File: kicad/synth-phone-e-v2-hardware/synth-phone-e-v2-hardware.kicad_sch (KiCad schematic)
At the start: 29 parts, among them J1 AudioJack4, J10 Audio_out_input, J11 mic_gain_input, J13 Audio_in_output, J14 Audio_out_output, J15 encoder_input, J2 AudioJack4, J3 DIN-5, J4 Keypad_column_output, J6 USB_C_Receptacle_USB2.0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

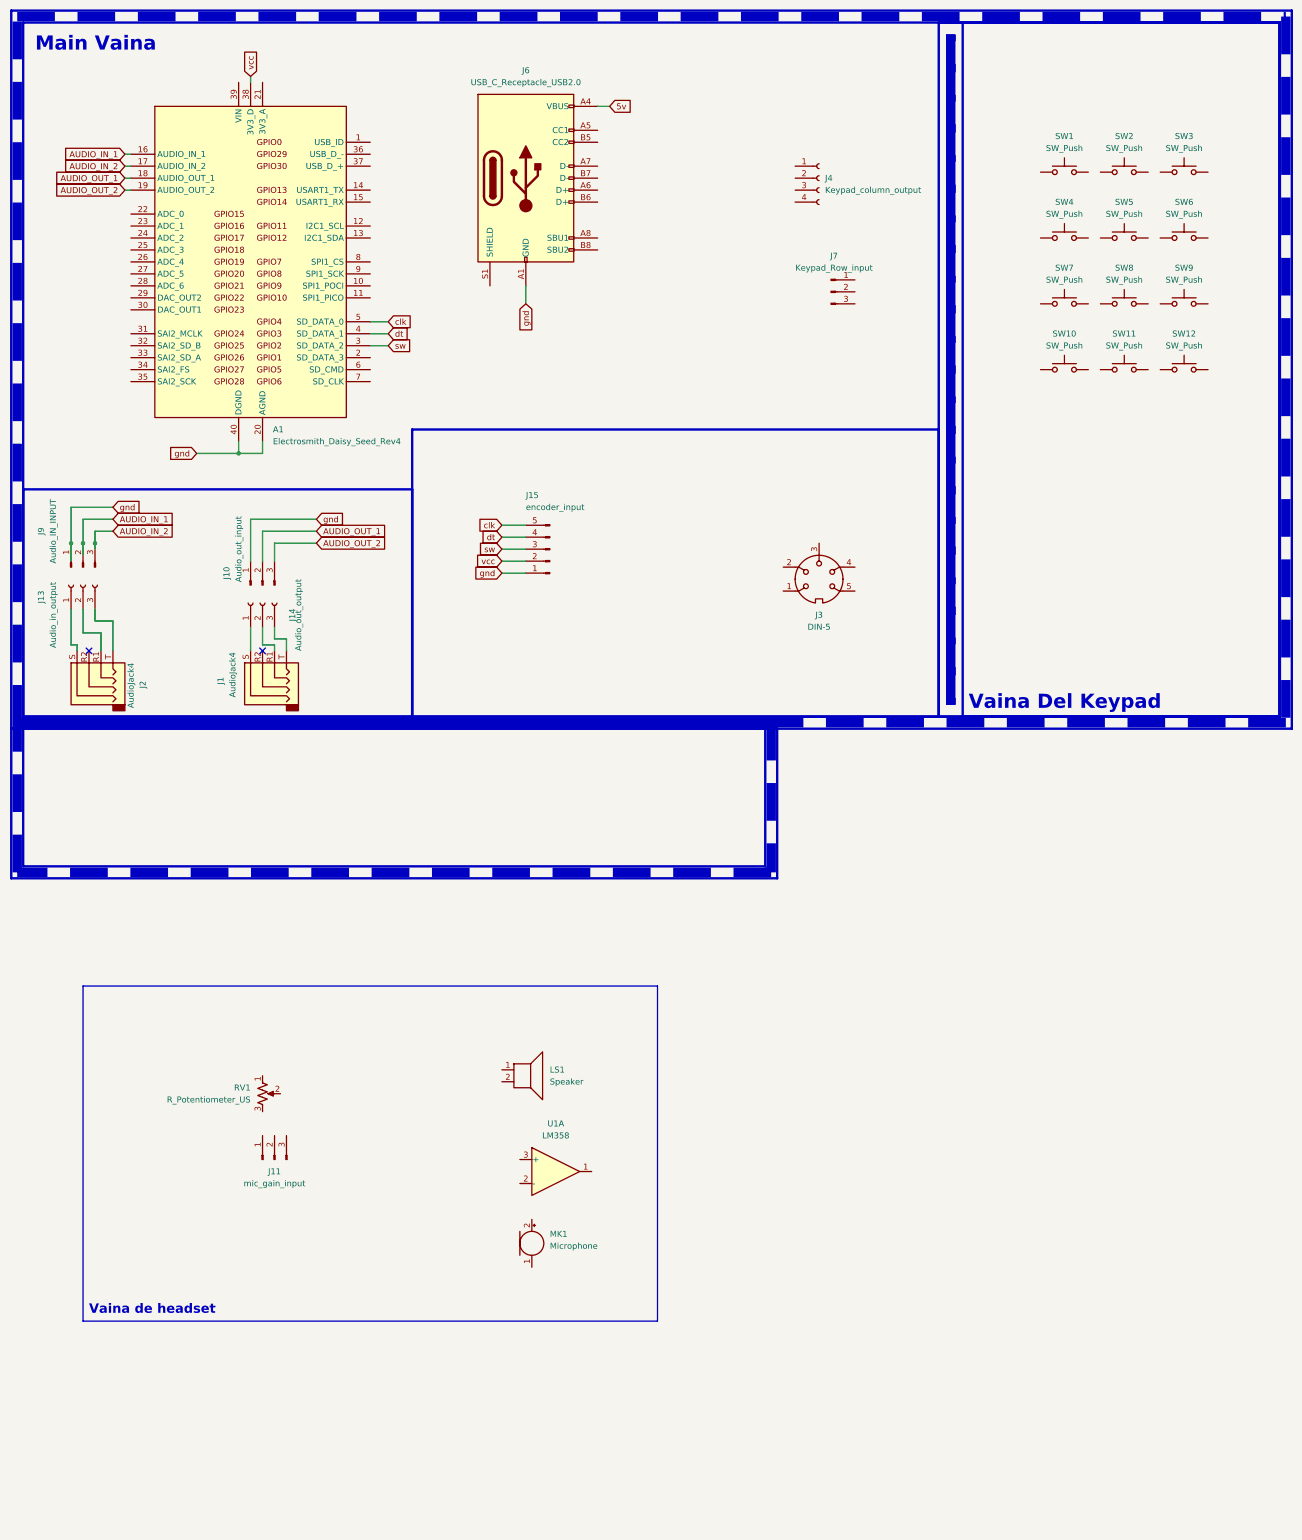
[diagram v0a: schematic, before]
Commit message: feat: encoder state machine
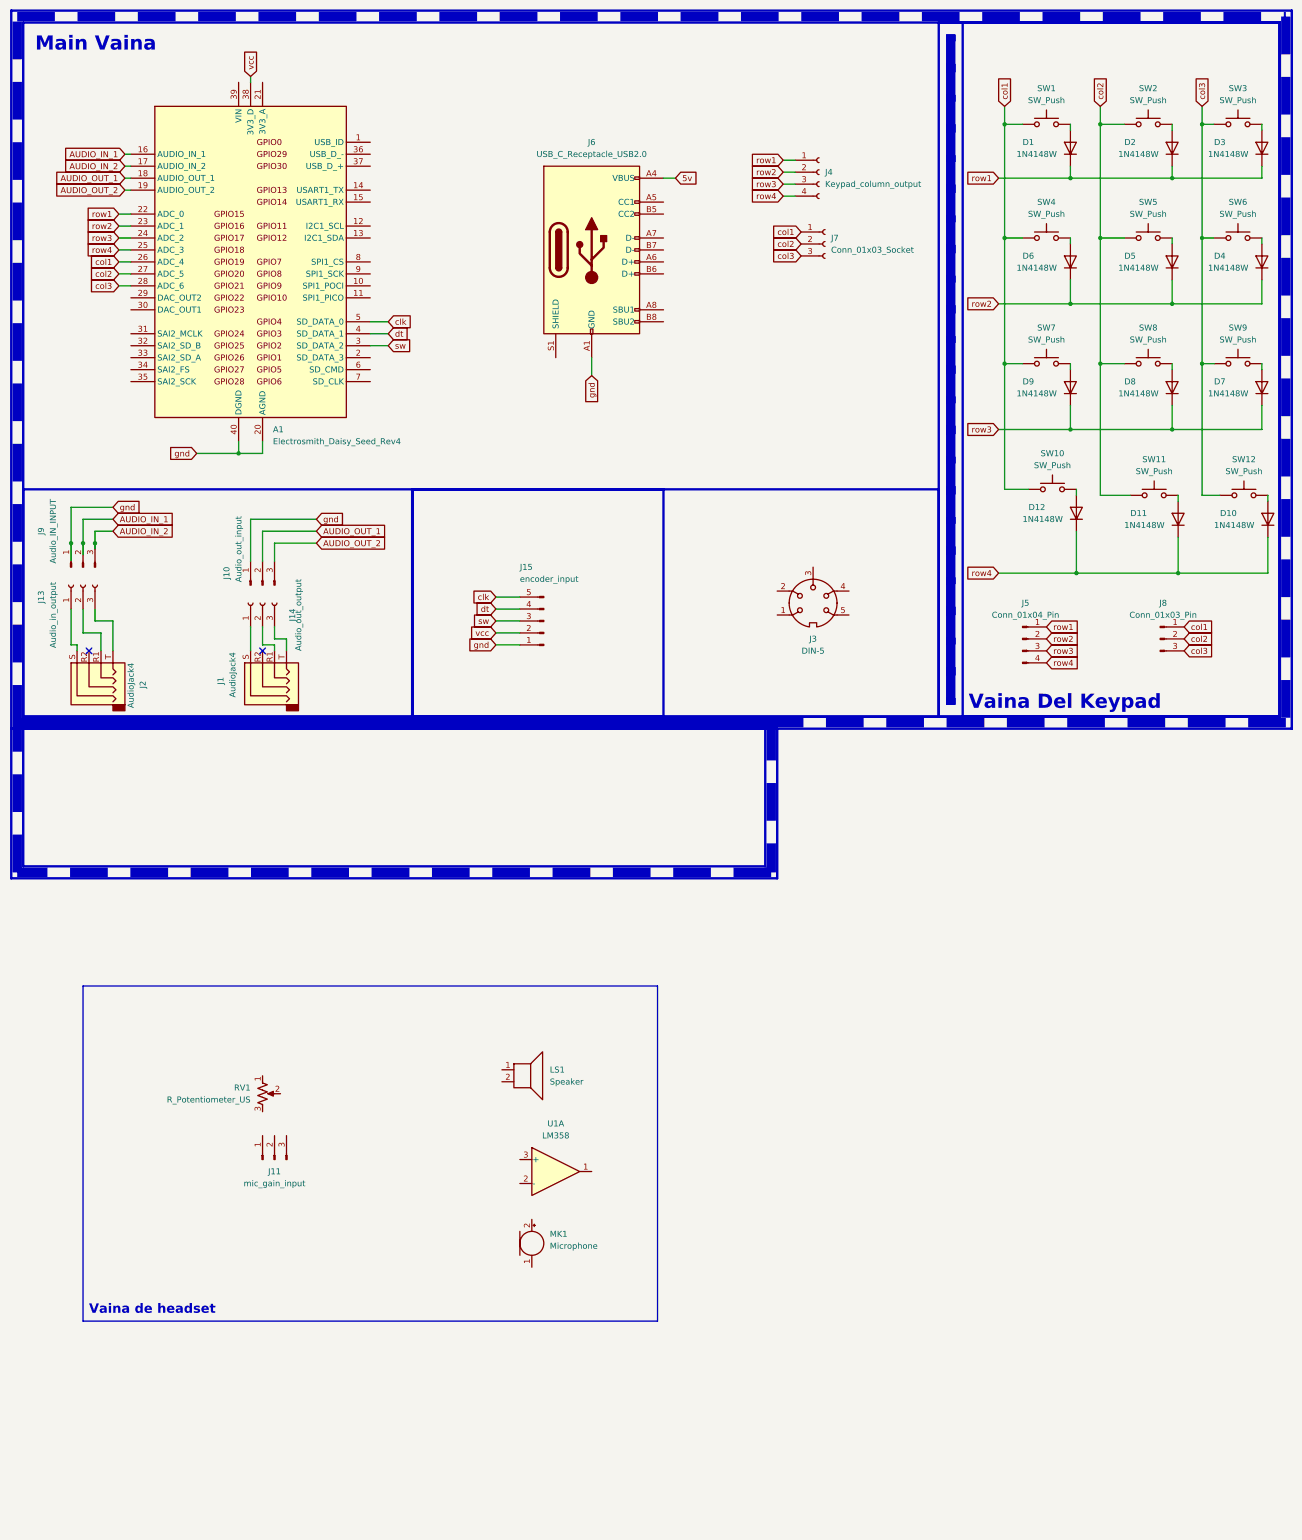
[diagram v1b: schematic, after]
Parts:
- removed J7: Keypad_Row_input, symbol Connector:Conn_01x03_Pin
- added D1, D10, D11, D12, D2, D3, D4, D5, D6, D7, D8, D9: 1N4148W, Diode_SMD:D_SOD-123, symbol Diode:1N4148W
- added J5: Conn_01x04_Pin, symbol Connector:Conn_01x04_Pin
- added J7: Conn_01x03_Socket, symbol Connector:Conn_01x03_Socket
- added J8: Conn_01x03_Pin, symbol Connector:Conn_01x03_Pin
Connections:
- net col1: now reaches SW4.1
- net col1: now also A1.26 (ADC_4), SW1.1, SW10.1, SW7.1, J7.1 (Pin_1), J8.1 (Pin_1)
- net at SW4.2: now also D6.2 (A)
- net col3: now reaches SW6.1
- net col3: now also A1.28 (ADC_6), SW12.1, SW3.1, SW9.1, J7.3 (Pin_3), J8.3 (Pin_3)
- net at SW6.2: now also D4.2 (A)
- net col2: now reaches SW8.1
- net col2: now also A1.27 (ADC_5), SW11.1, SW2.1, SW5.1, J7.2 (Pin_2), J8.2 (Pin_2)
- net at SW8.2: now also D8.2 (A)
- net row1: now reaches J4.1 (Pin_1)
- net row1: now also A1.22 (ADC_0), D1.1 (K), D2.1 (K), D3.1 (K), J5.1 (Pin_1)
- net row2: now reaches J4.2 (Pin_2)
- net row2: now also A1.23 (ADC_1), D4.1 (K), D5.1 (K), D6.1 (K), J5.2 (Pin_2)
- net row3: now reaches J4.3 (Pin_3)
- net row3: now also A1.24 (ADC_2), D7.1 (K), D8.1 (K), D9.1 (K), J5.3 (Pin_3)
- net row4: now reaches J4.4 (Pin_4)
- net row4: now also A1.25 (ADC_3), D10.1 (K), D11.1 (K), D12.1 (K), J5.4 (Pin_4)
- net at SW10.2: now also D12.2 (A)
- net at SW7.2: now also D9.2 (A)
- net at SW5.2: now also D5.2 (A)
- net at SW9.2: now also D7.2 (A)
- net at SW12.2: now also D10.2 (A)
- net at SW1.2: now also D1.2 (A)
- net at SW3.2: now also D3.2 (A)
- net at SW2.2: now also D2.2 (A)
- net at SW11.2: now also D11.2 (A)
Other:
- moved on the sheet: J15, J3, J4, J6, SW1, SW10, SW11, SW12, SW2, SW3, SW4, SW5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

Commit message: feat: basic lcd
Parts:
- added J12: display_socket, symbol Connector:Conn_01x04_Socket
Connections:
- net gnd: now also J12.4 (Pin_4)
- net vcc: now also J12.3 (Pin_3)
- net SCL: now reaches A1.12 (I2C1_SCL)
- net SCL: now also J12.2 (Pin_2)
- net SDA: now reaches A1.13 (I2C1_SDA)
- net SDA: now also J12.1 (Pin_1)

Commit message: chore: update schematic
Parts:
- added D13: 1N4148, Diode_THT:D_DO-35_SOD27_P7.62mm_Horizontal, symbol Diode:1N4148
- added J16: 4P4C, symbol Connector:4P4C
- added R1, R4, R5: R_US, symbol Device:R_US
- added SW13: SW_Wuerth_450301014042, Button_Switch_THT:SW_Slide-03_Wuerth-WS-SLTV_10x2.5x6.4_P2.54mm, symbol Switch:SW_Wuerth_450301014042
- added SW14: Audio Selector, symbol Switch:SW_Push_DPDT
- added U2: 6N138, symbol Isolator:6N138
- J5: value Conn_01x04_Pin -> keypad_row
- J8: value Conn_01x03_Pin -> keypad_col
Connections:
- net AUDIO_OUT_1: now also SW14.2 (B)
- net AUDIO_OUT_2: now also SW14.5 (B)
- net gnd: now also J3.3, J16.1, J16.2, R4.1, U2.5 (GND)
- net vcc: now also R5.2, U2.8 (VCC)
- net at J3.2: now also R1.1
- net at J3.4: now also D13.1 (K), U2.3 (C2)
- net MIDI_in_device: now reaches A1.15 (USART1_RX)
- net MIDI_in_device: now also R5.1, U2.6 (VO2)
- net AUDIO_IN_1 renamed AUDIO_IN_1_device
- net AUDIO_IN_1_device: no longer J9.2 (Pin_2)
- net AUDIO_IN_2 renamed AUDIO_IN_2_device
- net AUDIO_IN_2_device: no longer J9.3 (Pin_3)
- new net: R4.2, U2.7 (VO1)
- new net: J16.3, SW13.3 (A)
- new net: J16.4, SW13.2 (C)
- new net: D13.2 (A), R1.2, U2.2 (C1)
- new net AUDIO_IN_1_4p4c: SW13.1 (B), SW14.3 (C), SW14.6 (C)
- new net AUDIO_IN_1_jack: J9.2 (Pin_2), SW14.1 (A)
- new net AUDIO_IN_2_jack: J9.3 (Pin_3), SW14.4 (A)
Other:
- note added: "- Compressor pot (onboard)"
- note added: "- Gain pot (external)"
- note added: "- Power in circuitry"
- note added: "- Pre-Amp board"
- note added: "Jerk wants his cake and to eat it."
- note added: "Somehow make it possible to add a speaker and still do the same thing so that we he sees its a bad idea we arn't jodidos"
- note added: "Vaina Del MIDI"
- note added: "WONT DO"
- note removed: "Vaina Del Keypad"
- note removed: "Vaina de headset"
- moved on the sheet: D1, D10, D11, D12, D2, D3, D4, D5, D6, D7, D8, D9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

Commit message: chore: wip circuit board
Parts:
- removed D1, D10, D11, D12, D2, D3, D4, D5, D6, D7, D8, D9: 1N4148W, Diode_SMD:D_SOD-123, symbol Diode:1N4148W
- removed J10: Audio_out_input, symbol Connector:Conn_01x03_Pin
- removed J11: mic_gain_input, symbol Connector:Conn_01x03_Pin
- removed J13: Audio_in_output, symbol Connector:Conn_01x03_Socket
- removed J14: Audio_out_output, symbol Connector:Conn_01x03_Socket
- removed J5: keypad_row, symbol Connector:Conn_01x04_Pin
- removed J6: USB_C_Receptacle_USB2.0, Connector_USB:USB_C_Receptacle_GCT_USB4105-xx-A_16P_TopMnt_Horizontal, symbol Connector:USB_C_Receptacle_USB2.0
- removed J9: Audio_IN_INPUT, symbol Connector:Conn_01x03_Pin
- removed LS1: Speaker, symbol Device:Speaker
- removed MK1: Microphone, symbol Device:Microphone
- removed RV1: R_Potentiometer_US, symbol Device:R_Potentiometer_US
- removed SW1, SW10, SW11, SW12, SW2, SW3, SW4, SW5, SW6, SW7, SW8, SW9: SW_Push, symbol Switch:SW_Push
- removed SW14: Audio Selector, symbol Switch:SW_Push_DPDT
- removed U1: LM358, symbol Amplifier_Operational:LM358
- added J5: Jack-in, Connector_JST:JST_PH_B3B-PH-K_1x03_P2.00mm_Vertical, symbol Connector:Conn_01x03_Pin
- added J6: keypad socket, Connector_JST:JST_PH_B7B-PH-K_1x07_P2.00mm_Vertical, symbol Connector:Conn_01x07_Socket
- added R2, R3: ?, Resistor_THT:R_Axial_DIN0207_L6.3mm_D2.5mm_P15.24mm_Horizontal, symbol Device:R_US
- added RV2, RV3: R_Potentiometer_Trim_US, Connector_JST:JST_PH_B3B-PH-K_1x03_P2.00mm_Vertical, symbol Device:R_Potentiometer_Trim_US
- added SW14: SW_Push_SPDT, Connector_JST:JST_PH_B3B-PH-K_1x03_P2.00mm_Vertical, symbol Switch:SW_Push_SPDT
- added U3: ~, koobook:ssm2167, symbol koobook_pre_amp:SSM2167
- J12, J16: footprint (none) -> Connector_JST:JST_PH_B4B-PH-K_1x04_P2.00mm_Vertical
- J15, J3: footprint (none) -> Connector_JST:JST_PH_B5B-PH-K_1x05_P2.00mm_Vertical
- J4: footprint (none) -> Connector_PinSocket_2.54mm:PinSocket_1x04_P2.54mm_Vertical
- J7: value Conn_01x03_Socket -> keypad_row_output; footprint (none) -> Connector_PinSocket_2.54mm:PinSocket_1x03_P2.54mm_Vertical
- J8: value keypad_col -> jack-out; footprint (none) -> Connector_JST:JST_PH_B3B-PH-K_1x03_P2.00mm_Vertical
- R1, R5: value R_US -> 220; footprint (none) -> Resistor_THT:R_Axial_DIN0207_L6.3mm_D2.5mm_P15.24mm_Horizontal
- R4: value R_US -> 4.7k; footprint (none) -> Resistor_THT:R_Axial_DIN0207_L6.3mm_D2.5mm_P15.24mm_Horizontal
- U2: footprint (none) -> Package_DIP:DIP-8_W7.62mm
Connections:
- net AUDIO_IN_2_device is gone; now on net AUDIO_IN_1_jack: A1.17 (AUDIO_IN_2)
- net AUDIO_IN_1_4p4c: now also R2.2, R3.2, U3.3 (IN+)
- net AUDIO_IN_1_jack: now also J2.R1, J2.T, J5.1 (Pin_1), J5.2 (Pin_2)
- net AUDIO_OUT_1: now also J1.R1, J8.2 (Pin_2)
- net AUDIO_OUT_2: now also J1.T, J8.1 (Pin_1)
- net col1: now also J6.3 (Pin_3); no longer J8.1 (Pin_1)
- net col2: now also J6.2 (Pin_2); no longer J8.2 (Pin_2)
- net col3: now also J6.1 (Pin_1); no longer J8.3 (Pin_3)
- net gnd: now also J1.S, J2.S, J8.3 (Pin_3), J5.3 (Pin_3), R2.1, R3.1, SW14.3 (C), U3.2 (gnd), U3.4 (IN-), U3.6 (OUT-)
- net row1: now also J6.7 (Pin_7)
- net row2: now also J6.6 (Pin_6)
- net row3: now also J6.5 (Pin_5)
- net row4: now also J6.4 (Pin_4)
- net vcc: now also SW14.1 (A), U3.1 (vcc)
- net channel_selector: now reaches A1.2 (SD_DATA_3)
- net channel_selector: now also SW14.2 (B)
- net AUDIO_IN_1_device renamed AUDIO_IN_AMP
- net AUDIO_IN_AMP: now also U3.5 (OUT+)
- new net: RV3.1, U3.9 (R2R)
- new net: RV3.2, U3.8 (R2M)
- new net: RV3.3, U3.7 (R2L)
- new net: RV2.1, U3.12 (R1R)
- new net: RV2.2, U3.11 (R1M)
- new net: RV2.3, U3.10 (R1L)
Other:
- note removed: "- Compressor pot (onboard)"
- note removed: "- Gain pot (external)"
- note removed: "- Power in circuitry"
- note removed: "- Pre-Amp board"
- note removed: "WONT DO"
- moved on the sheet: A1, J12, J3, J4, J7

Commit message: feat: finish pcb
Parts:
- removed R3: ?, Resistor_THT:R_Axial_DIN0207_L6.3mm_D2.5mm_P15.24mm_Horizontal, symbol Device:R_US
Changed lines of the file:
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@@
 	)
 	(junction
-		(at 189.23 130.81)
-		(diameter 0)
-		(color 0 0 0 0)
-	)
-	(junction
 		(at 30.48 120.65)
 		(diameter 0)
@@
 	)
 	(junction
-		(at 189.23 138.43)
-		(diameter 0)
-		(color 0 0 0 0)
-	)
-	(junction
 		(at 274.32 109.22)
 		(diameter 0)
@@
 	(wire
 		(pts
-			(xy 189.23 138.43) (xy 199.39 138.43)
-		)
-		(stroke
-			(width 0)
-			(type default)
-		)
-	)
-	(wire
-		(pts
 			(xy 115.57 147.32) (xy 120.65 147.32)
 		)
@@
 	(wire
 		(pts
-			(xy 189.23 130.81) (xy 190.5 130.81)
+			(xy 187.96 130.81) (xy 190.5 130.81)
 		)
 		(stroke
@@
 	(wire
 		(pts
-			(xy 180.34 138.43) (xy 189.23 138.43)
+			(xy 180.34 138.43) (xy 199.39 138.43)
 		)
 		(stroke
@@
 	(wire
 		(pts
-			(xy 189.23 130.81) (xy 187.96 130.81)
-		)
-		(stroke
-			(width 0)
-			(type default)
-		)
-	)
-	(wire
-		(pts
 			(xy 63.5 132.08) (xy 63.5 148.59)
 		)
@@
 					(unit 1)
 				)
-			)
-		)
-	)
-	(symbol
-		(lib_id "Device:R_US")
-		(at 189.23 134.62 180)
-		(unit 1)
-		(exclude_from_sim no)
-		(in_bom yes)
-		(on_board yes)
-		(dnp no)
-		(fields_autoplaced yes)
-		(property "Reference" "R3"
-			(at 191.77 133.3499 0)
-			(effects
-				(font
-					(size 1.27 1.27)
-				)
-				(justify right)
-			)
-		)
-		(property "Value" "?"
-			(at 191.77 135.8899 0)
-			(effects
-				(font
-					(size 1.27 1.27)
-				)
-				(justify right)
-			)
-		)
-		(property "Footprint" "Resistor_THT:R_Axial_DIN0207_L6.3mm_D2.5mm_P15.24mm_Horizontal"
-			(at 188.214 134.366 90)
-			(effects
-				(font
-					(size 1.27 1.27)
-				)
-				(hide yes)
-			)
-		)
-		(property "Datasheet" "~"
-			(at 189.23 134.62 0)
-			(effects
-				(font
-					(size 1.27 1.27)
-				)
-				(hide yes)
-			)
-		)
-		(property "Description" "Resistor, US symbol"
-			(at 189.23 134.62 0)
-			(effects
-				(font
-					(size 1.27 1.27)
-				)
-				(hide yes)
-			)
-		)
-		(pin "2"
-		)
-		(pin "1"
-		)
-		(instances
-			(project "synth-phone-e-v2-hardware"
-				(path "/75d2a775-5539-423d-a5af-ebbe708c65a6"
-					(reference "R3")
-					(unit 1)
-				)

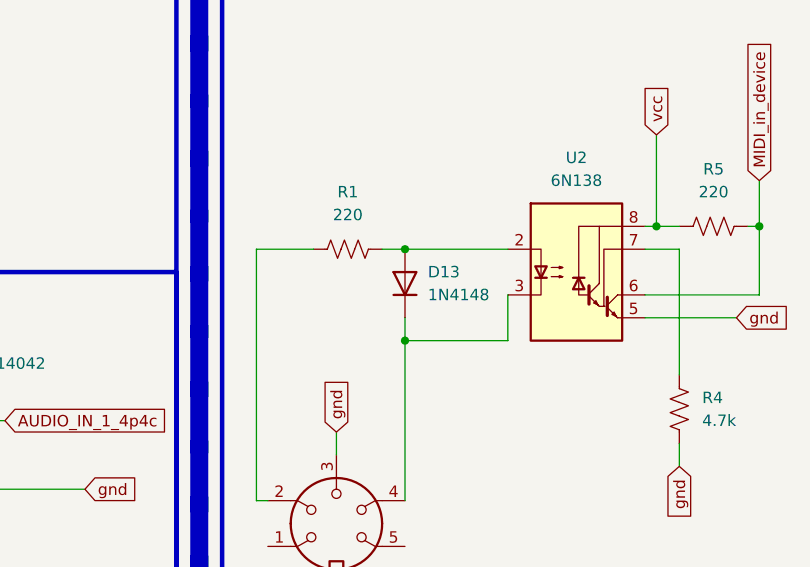
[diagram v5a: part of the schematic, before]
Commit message: feat: basic midi support
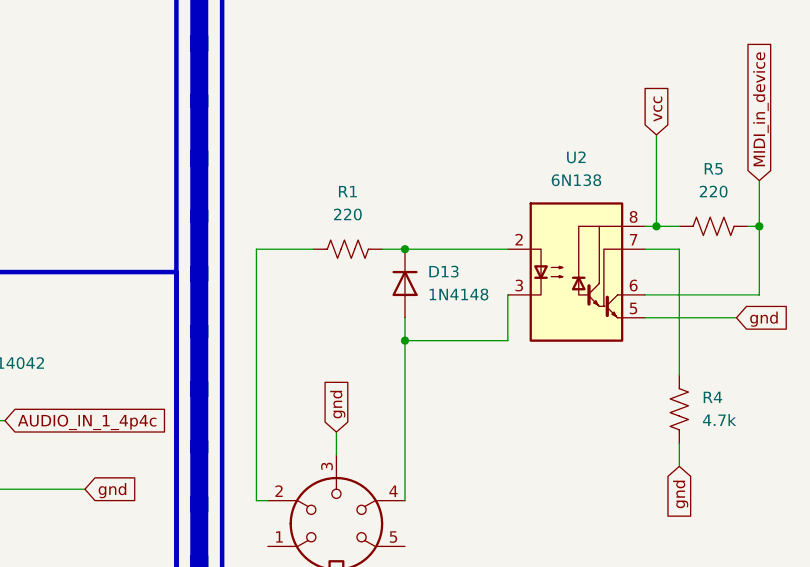
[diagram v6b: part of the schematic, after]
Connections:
- net at J3.4, U2.3 (C2): now also D13.2 (A); no longer D13.1 (K)
- net at R1.2, U2.2 (C1): now also D13.1 (K); no longer D13.2 (A)
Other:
- moved on the sheet: D13
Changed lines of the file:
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@@
 	)
 	(junction
-		(at 234.95 111.76)
+		(at 180.34 138.43)
 		(diameter 0)
 		(color 0 0 0 0)
 	)
 	(junction
-		(at 180.34 138.43)
+		(at 58.42 106.68)
 		(diameter 0)
 		(color 0 0 0 0)
 	)
 	(junction
-		(at 58.42 106.68)
+		(at 262.89 109.22)
 		(diameter 0)
 		(color 0 0 0 0)
 	)
 	(junction
-		(at 262.89 109.22)
+		(at 234.95 111.76)
 		(diameter 0)
 		(color 0 0 0 0)
@@
 	(wire
 		(pts
+			(xy 234.95 111.76) (xy 246.38 111.76)
+		)
+		(stroke
+			(width 0)
+			(type default)
+		)
+	)
+	(wire
+		(pts
 			(xy 227.33 58.42) (xy 231.14 58.42)
 		)
@@
 	(wire
 		(pts
-			(xy 234.95 111.76) (xy 246.38 111.76)
-		)
-		(stroke
-			(width 0)
-			(type default)
-		)
-	)
-	(wire
-		(pts
 			(xy 86.36 83.82) (xy 87.63 83.82)
 		)
@@
 	(symbol
 		(lib_id "Diode:1N4148")
-		(at 234.95 115.57 90)
+		(at 234.95 115.57 270)
 		(unit 1)
 		(exclude_from_sim no)
@@
 					(size 1.27 1.27)
 				)
-				(justify right)
+				(justify left)
 			)
 		)
@@
 					(size 1.27 1.27)
 				)
-				(justify right)
+				(justify left)
 			)
 		)
